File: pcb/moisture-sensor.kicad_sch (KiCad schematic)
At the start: 35 parts, among them J3 USB4110, U1 ESP32-C3-WROOM-02, U2 TPS631000, U4 MCP73832, Y1 32.768kHz

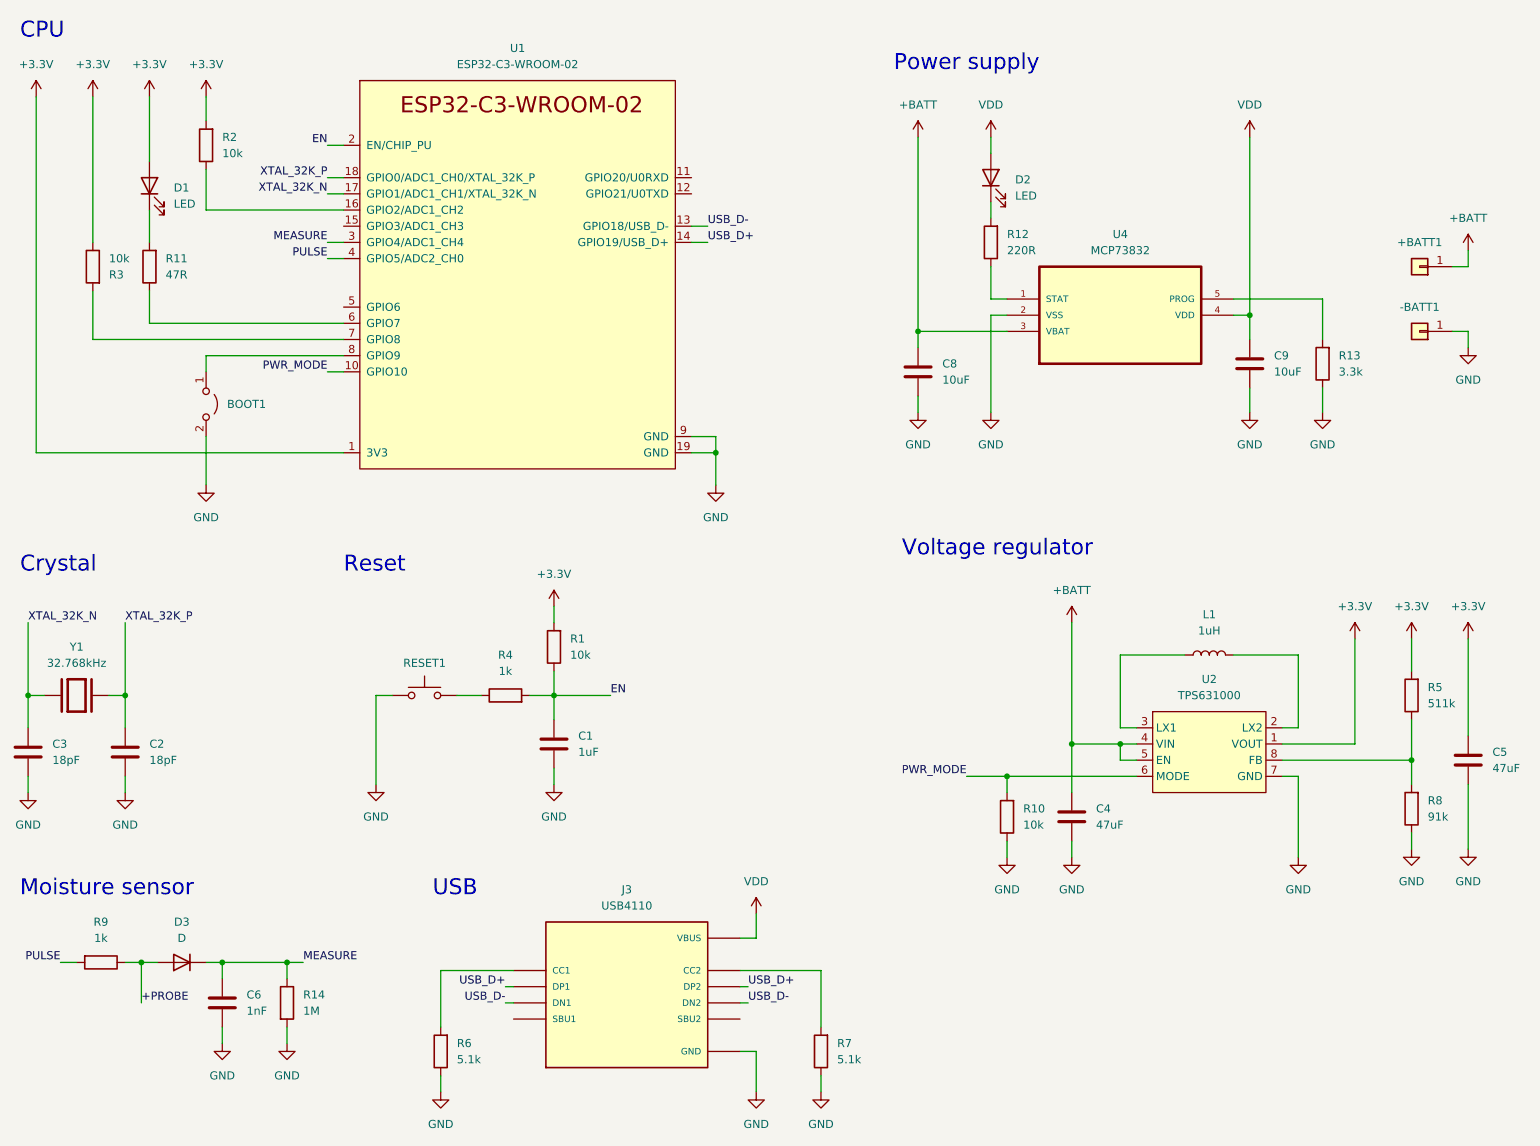
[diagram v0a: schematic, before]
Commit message: prefer built in KiCad items
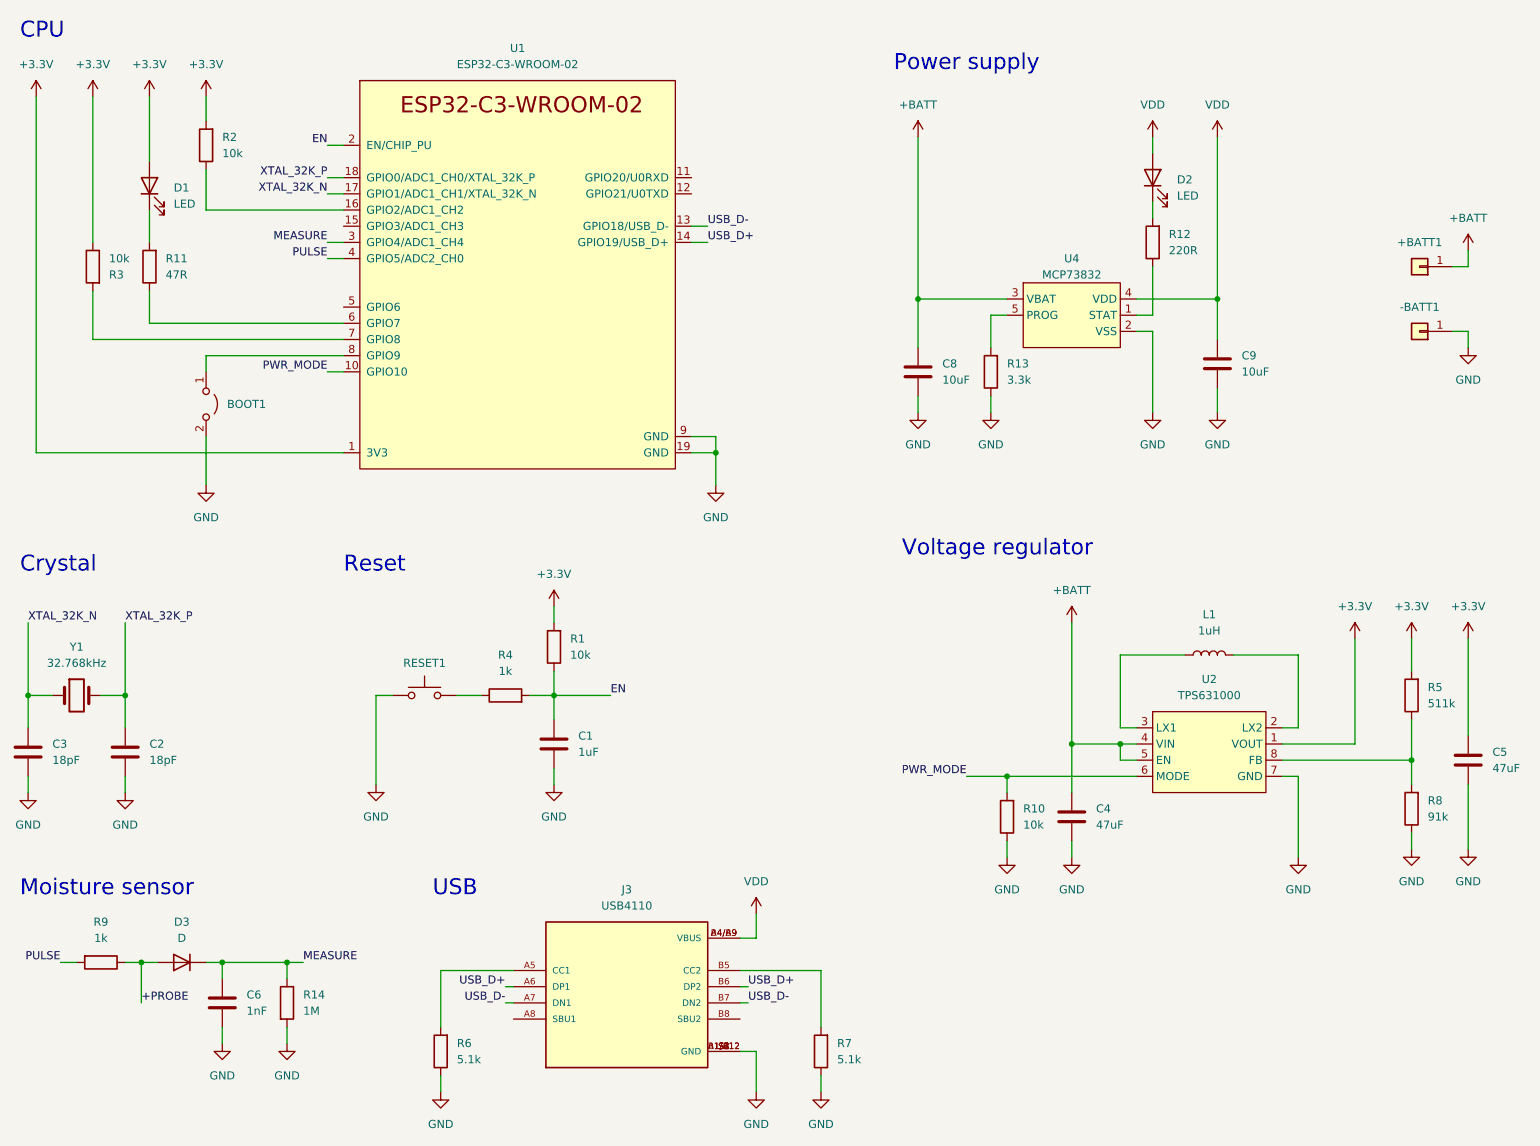
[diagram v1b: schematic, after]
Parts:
- J3: footprint library:GCT_USB4110-GF-A_REVB -> library:USB4110-GF-A_REVB
- U4: symbol MCP73832T-4ADI_OT:MCP73832T-4ADI/OT -> friedrich:MCP73831/2
- Y1: footprint library:ABS07-32.768KHZ-T -> Crystal:Crystal_SMD_G8-2Pin_3.2x1.5mm_HandSoldering; symbol ABS07-32.768KHZ-1-T:ABS07-32.768KHZ-1-T -> Device:Crystal
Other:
- moved on the sheet: C9, D2, R12, R13, U4

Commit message: increase power supply capacitor sizes
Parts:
- C8, C9: value 10uF -> 47uF; MPN GRM21BR71A106KA73 -> GRM21BR61A476ME15
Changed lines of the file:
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@@
       (effects (font (size 1.27 1.27)) (justify right))
     )
-    (property "Value" "10uF" (id 1) (at 214.63 73.6599 0)
+    (property "Value" "47uF" (id 1) (at 214.63 73.6599 0)
       (effects (font (size 1.27 1.27)) (justify right))
     )
@@
       (effects (font (size 1.27 1.27)) hide)
     )
-    (property "MPN" "GRM21BR71A106KA73" (id 4) (at 210.82 72.39 0)
+    (property "MPN" "GRM21BR61A476ME15" (id 4) (at 210.82 72.39 0)
       (effects (font (size 1.27 1.27)) hide)
     )
@@
       (effects (font (size 1.27 1.27)) (justify right))
     )
-    (property "Value" "10uF" (id 1) (at 167.64 74.9299 0)
+    (property "Value" "47uF" (id 1) (at 167.64 74.9299 0)
       (effects (font (size 1.27 1.27)) (justify right))
     )
@@
       (effects (font (size 1.27 1.27)) hide)
     )
-    (property "MPN" "GRM21BR71A106KA73" (id 4) (at 163.83 73.66 0)
+    (property "MPN" "GRM21BR61A476ME15" (id 4) (at 163.83 73.66 0)
       (effects (font (size 1.27 1.27)) hide)
     )
@@
     )
     (path "/d17c0af9-46e4-46cc-916e-89295d85b16e"
-      (reference "C8") (unit 1) (value "10uF") (footprint "Capacitor_SMD:C_0805_2012Metric_Pad1.18x1.45mm_HandSolder")
+      (reference "C8") (unit 1) (value "47uF") (footprint "Capacitor_SMD:C_0805_2012Metric_Pad1.18x1.45mm_HandSolder")
     )
     (path "/c2babd92-eafd-4e03-91b8-aea8d8099d2a"
-      (reference "C9") (unit 1) (value "10uF") (footprint "Capacitor_SMD:C_0805_2012Metric_Pad1.18x1.45mm_HandSolder")
+      (reference "C9") (unit 1) (value "47uF") (footprint "Capacitor_SMD:C_0805_2012Metric_Pad1.18x1.45mm_HandSolder")
     )
     (path "/f0353968-959d-47cb-85e9-234a9c0fc1de"

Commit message: Revert "increase power supply capacitor sizes"
This reverts commit e628d20ff7827fca777ef456cf9c7b65b2cb21d5.
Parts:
- C8, C9: value 47uF -> 10uF; MPN GRM21BR61A476ME15 -> GRM21BR71A106KA73
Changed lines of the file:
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@@
       (effects (font (size 1.27 1.27)) (justify right))
     )
-    (property "Value" "47uF" (id 1) (at 214.63 73.6599 0)
+    (property "Value" "10uF" (id 1) (at 214.63 73.6599 0)
       (effects (font (size 1.27 1.27)) (justify right))
     )
@@
       (effects (font (size 1.27 1.27)) hide)
     )
-    (property "MPN" "GRM21BR61A476ME15" (id 4) (at 210.82 72.39 0)
+    (property "MPN" "GRM21BR71A106KA73" (id 4) (at 210.82 72.39 0)
       (effects (font (size 1.27 1.27)) hide)
     )
@@
       (effects (font (size 1.27 1.27)) (justify right))
     )
-    (property "Value" "47uF" (id 1) (at 167.64 74.9299 0)
+    (property "Value" "10uF" (id 1) (at 167.64 74.9299 0)
       (effects (font (size 1.27 1.27)) (justify right))
     )
@@
       (effects (font (size 1.27 1.27)) hide)
     )
-    (property "MPN" "GRM21BR61A476ME15" (id 4) (at 163.83 73.66 0)
+    (property "MPN" "GRM21BR71A106KA73" (id 4) (at 163.83 73.66 0)
       (effects (font (size 1.27 1.27)) hide)
     )
@@
     )
     (path "/d17c0af9-46e4-46cc-916e-89295d85b16e"
-      (reference "C8") (unit 1) (value "47uF") (footprint "Capacitor_SMD:C_0805_2012Metric_Pad1.18x1.45mm_HandSolder")
+      (reference "C8") (unit 1) (value "10uF") (footprint "Capacitor_SMD:C_0805_2012Metric_Pad1.18x1.45mm_HandSolder")
     )
     (path "/c2babd92-eafd-4e03-91b8-aea8d8099d2a"
-      (reference "C9") (unit 1) (value "47uF") (footprint "Capacitor_SMD:C_0805_2012Metric_Pad1.18x1.45mm_HandSolder")
+      (reference "C9") (unit 1) (value "10uF") (footprint "Capacitor_SMD:C_0805_2012Metric_Pad1.18x1.45mm_HandSolder")
     )
     (path "/f0353968-959d-47cb-85e9-234a9c0fc1de"

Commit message: add battery voltage measurement
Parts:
- added R? (x2): 1M, symbol Device:R
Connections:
- net +BATT: now also R?.1
- net GND: now also R?.2
- net HALF_BATT: now reaches U1.15 (GPIO3/ADC1_CH3)
- net HALF_BATT: now also R?.1, R?.2
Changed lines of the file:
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@@
   (junction (at 64.77 166.37) (diameter 0) (color 0 0 0 0)
   )
+  (junction (at 143.51 120.65) (diameter 0) (color 0 0 0 0)
+  )
   (junction (at 187.96 132.08) (diameter 0) (color 0 0 0 0)
   )
@@
     (stroke (width 0) (type default) (color 0 0 0 0))
   )
+  (wire (pts (xy 71.12 50.8) (xy 73.66 50.8))
+    (stroke (width 0) (type default) (color 0 0 0 0))
+  )
   (wire (pts (xy 200.66 46.99) (xy 200.66 49.53))
     (stroke (width 0) (type default) (color 0 0 0 0))
@@
     (stroke (width 0) (type default) (color 0 0 0 0))
   )
+  (wire (pts (xy 143.51 118.11) (xy 143.51 120.65))
+    (stroke (width 0) (type default) (color 0 0 0 0))
+  )
   (wire (pts (xy 132.08 83.82) (xy 132.08 86.36))
     (stroke (width 0) (type default) (color 0 0 0 0))
@@
     (stroke (width 0) (type default) (color 0 0 0 0))
   )
+  (wire (pts (xy 143.51 130.81) (xy 143.51 133.35))
+    (stroke (width 0) (type default) (color 0 0 0 0))
+  )
   (wire (pts (xy 241.3 115.57) (xy 241.3 120.65))
     (stroke (width 0) (type default) (color 0 0 0 0))
@@
     (stroke (width 0) (type default) (color 0 0 0 0))
   )
+  (wire (pts (xy 143.51 107.95) (xy 143.51 110.49))
+    (stroke (width 0) (type default) (color 0 0 0 0))
+  )
   (wire (pts (xy 64.77 176.53) (xy 64.77 179.07))
     (stroke (width 0) (type default) (color 0 0 0 0))
@@
     (stroke (width 0) (type default) (color 0 0 0 0))
   )
+  (wire (pts (xy 143.51 120.65) (xy 143.51 123.19))
+    (stroke (width 0) (type default) (color 0 0 0 0))
+  )
   (wire (pts (xy 24.13 137.16) (xy 24.13 139.7))
     (stroke (width 0) (type default) (color 0 0 0 0))
@@
   )
   (wire (pts (xy 29.21 166.37) (xy 31.75 166.37))
+    (stroke (width 0) (type default) (color 0 0 0 0))
+  )
+  (wire (pts (xy 143.51 120.65) (xy 146.05 120.65))
     (stroke (width 0) (type default) (color 0 0 0 0))
   )
@@
     (effects (font (size 1.27 1.27)) (justify left bottom))
   )
+  (label "HALF_BATT" (at 146.05 120.65 0)
+    (effects (font (size 1.27 1.27)) (justify left bottom))
+  )
   (label "EN" (at 71.12 38.1 180)
     (effects (font (size 1.27 1.27)) (justify right bottom))
@@
   )
   (label "PULSE" (at 29.21 166.37 180)
+    (effects (font (size 1.27 1.27)) (justify right bottom))
+  )
+  (label "HALF_BATT" (at 71.12 50.8 180)
     (effects (font (size 1.27 1.27)) (justify right bottom))
   )
@@
     (pin "1")
   )
+  (symbol (lib_id "power:+BATT") (at 143.51 107.95 0) (unit 1)
+    (in_bom yes) (on_board yes) (fields_autoplaced)
+    (property "Reference" "#PWR?" (id 0) (at 143.51 111.76 0)
+      (effects (font (size 1.27 1.27)) hide)
+    )
+    (property "Value" "+BATT" (id 1) (at 143.51 102.87 0))
+    (property "Footprint" "" (id 2) (at 143.51 107.95 0)
+      (effects (font (size 1.27 1.27)) hide)
+    )
+    (property "Datasheet" "" (id 3) (at 143.51 107.95 0)
+      (effects (font (size 1.27 1.27)) hide)
+    )
+    (pin "1")
+  )
   (symbol (lib_id "Device:C") (at 187.96 143.51 0) (unit 1)
     (in_bom yes) (on_board yes)
@@
     )
     (pin "1")
+  )
+  (symbol (lib_id "Device:R") (at 143.51 114.3 0) (unit 1)
+    (in_bom yes) (on_board yes) (fields_autoplaced)
+    (property "Reference" "R?" (id 0) (at 146.05 113.0299 0)
+      (effects (font (size 1.27 1.27)) (justify left))
+    )
+    (property "Value" "1M" (id 1) (at 146.05 115.5699 0)
+      (effects (font (size 1.27 1.27)) (justify left))
+    )
+    (property "Footprint" "" (id 2) (at 141.732 114.3 90)
+      (effects (font (size 1.27 1.27)) hide)
+    )
+    (property "Datasheet" "~" (id 3) (at 143.51 114.3 0)
+      (effects (font (size 1.27 1.27)) hide)
+    )
+    (pin "1")
+    (pin "2")
   )
   (symbol (lib_id "power:+3.3V") (at 241.3 115.57 0) (unit 1)
@@
     (pin "1")
   )
+  (symbol (lib_id "Device:R") (at 143.51 127 0) (unit 1)
+    (in_bom yes) (on_board yes) (fields_autoplaced)
+    (property "Reference" "R?" (id 0) (at 146.05 125.7299 0)
+      (effects (font (size 1.27 1.27)) (justify left))
+    )
+    (property "Value" "1M" (id 1) (at 146.05 128.2699 0)
+      (effects (font (size 1.27 1.27)) (justify left))
+    )
+    (property "Footprint" "" (id 2) (at 141.732 127 90)
+      (effects (font (size 1.27 1.27)) hide)
+    )
+    (property "Datasheet" "~" (id 3) (at 143.51 127 0)
+      (effects (font (size 1.27 1.27)) hide)
+    )
+    (pin "1")
+    (pin "2")
+  )
   (symbol (lib_id "power:+3.3V") (at 232.41 115.57 0) (unit 1)
     (in_bom yes) (on_board yes)
@@
     (pin "1")
     (pin "2")
+  )
+  (symbol (lib_id "power:GND") (at 143.51 133.35 0) (unit 1)
+    (in_bom yes) (on_board yes) (fields_autoplaced)
+    (property "Reference" "#PWR?" (id 0) (at 143.51 139.7 0)
+      (effects (font (size 1.27 1.27)) hide)
+    )
+    (property "Value" "GND" (id 1) (at 143.51 138.43 0))
+    (property "Footprint" "" (id 2) (at 143.51 133.35 0)
+      (effects (font (size 1.27 1.27)) hide)
+    )
+    (property "Datasheet" "" (id 3) (at 143.51 133.35 0)
+      (effects (font (size 1.27 1.27)) hide)
+    )
+    (pin "1")
   )
   (symbol (lib_id "Device:LED") (at 43.18 44.45 90) (unit 1)
@@
       (reference "#PWR0135") (unit 1) (value "+3.3V") (footprint "")
     )
+    (path "/ad4bcc5d-3c6c-4210-b38d-456be0fdab6b"
+      (reference "#PWR?") (unit 1) (value "+BATT") (footprint "")
+    )
+    (path "/ecfdcb2a-e028-4773-adc8-06647bd8c5d2"
+      (reference "#PWR?") (unit 1) (value "GND") (footprint "")
+    )
     (path "/f16350ea-43d8-48ac-aa07-395402bdea62"
       (reference "+BATT1") (unit 1) (value "Conn_01x01") (footprint "Connector_Wire:SolderWire-0.25sqmm_1x01_D0.65mm_OD1.7mm")
@@
       (reference "R14") (unit 1) (value "1M") (footprint "Resistor_SMD:R_0805_2012Metric_Pad1.20x1.40mm_HandSolder")
     )
+    (path "/d7cfa866-c132-4eea-880f-95ede4729b36"
+      (reference "R?") (unit 1) (value "1M") (footprint "")
+    )
+    (path "/e781a7a8-fb3d-41da-a71a-62a3424ff862"
+      (reference "R?") (unit 1) (value "1M") (footprint "")
+    )
     (path "/4d1b128f-a7a4-4f89-9e1f-a12bb17f1956"
